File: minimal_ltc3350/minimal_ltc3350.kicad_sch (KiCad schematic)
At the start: 0 parts

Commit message: Update KiCad project files (PCB layout, project settings, and schematic)
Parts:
- added U1: LTC3350EUHF-PBF, analog_devices_footprints:QFN-38_UHF_LIT, symbol UNITED_IC_ADI:U_LTC3350EUHF-PBF
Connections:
- new net GND: U1.39 (PGND)
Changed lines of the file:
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@@
 	(generator "eeschema")
 	(generator_version "9.0")
-	(paper "A4")
+	(paper "A3")
+	(wire
+		(pts
+			(xy 203.2 231.14) (xy 203.2 232.41)
+		)
+		(stroke
+			(width 0)
+			(type default)
+		)
+	)
+	(symbol
+		(lib_id "UNITED_IC_ADI:U_LTC3350EUHF-PBF")
+		(at 203.2 152.4 0)
+		(unit 1)
+		(exclude_from_sim no)
+		(in_bom yes)
+		(on_board yes)
+		(dnp no)
+		(fields_autoplaced yes)
+		(property "Reference" "U1"
+			(at 205.3433 231.14 0)
+			(effects
+				(font
+					(size 1.524 1.524)
+				)
+				(justify left)
+			)
+		)
+		(property "Value" "LTC3350EUHF-PBF"
+			(at 205.3433 233.68 0)
+			(effects
+				(font
+					(size 1.524 1.524)
+				)
+				(justify left)
+			)
+		)
+		(property "Footprint" "analog_devices_footprints:QFN-38_UHF_LIT"
+			(at 243.84 236.22 0)
+			(effects
+				(font
+					(size 1.27 1.27)
+					(italic yes)
+				)
+				(justify left)
+				(hide yes)
+			)
+		)
+		(property "Datasheet" "https://www.analog.com/media/en/technical-documentation/data-sheets/ltc3350.pdf"
+			(at 243.84 231.14 0)
+			(effects
+				(font
+					(size 1.27 1.27)
+					(italic yes)
+				)
+				(justify left)
+				(hide yes)
+			)
+		)
+		(property "Description" "High Current Supercapacitor Backup Controller and System Monitor"
+			(at 243.84 233.68 0)
+			(effects
+				(font
+					(size 1.27 1.27)
+				)
+				(justify left)
+				(hide yes)
+			)
+		)
+		(property "MPN" "LTC3350EUHF#PBF"
+			(at 243.84 238.76 0)
+			(effects
+				(font
+					(size 1.27 1.27)
+				)
+				(justify left)
+				(hide yes)
+			)
+		)
+		(pin "26"
+		)
+		(pin "22"
+		)
+		(pin "4"
+		)
+		(pin "34"
+		)
+		(pin "35"
+		)
+		(pin "18"
+		)
+		(pin "30"
+		)
+		(pin "37"
+		)
+		(pin "28"
+		)
+		(pin "33"
+		)
+		(pin "24"
+		)
+		(pin "39"
+		)
+		(pin "17"
+		)
+		(pin "19"
+		)
+		(pin "5"
+		)
+		(pin "25"
+		)
+		(pin "2"
+		)
+		(pin "16"
+		)
+		(pin "14"
+		)
+		(pin "23"
+		)
+		(pin "11"
+		)
+		(pin "31"
+		)
+		(pin "7"
+		)
+		(pin "9"
+		)
+		(pin "20"
+		)
+		(pin "10"
+		)
+		(pin "29"
+		)
+		(pin "27"
+		)
+		(pin "1"
+		)
+		(pin "21"
+		)
+		(pin "15"
+		)
+		(pin "13"
+		)
+		(pin "32"
+		)
+		(pin "12"
+		)
+		(pin "3"
+		)
+		(pin "38"
+		)
+		(pin "36"
+		)
+		(pin "8"
+		)
+		(pin "6"
+		)
+		(instances
+			(project ""
+				(path "/7082067f-79ec-4bdc-ac64-cad75a2d3be3"
+					(reference "U1")
+					(unit 1)
+				)
+			)
+		)
+	)
+	(symbol
+		(lib_id "power:GND")
+		(at 203.2 232.41 0)
+		(unit 1)
+		(exclude_from_sim no)
+		(in_bom yes)
+		(on_board yes)
+		(dnp no)
+		(fields_autoplaced yes)
+		(property "Reference" "#PWR01"
+			(at 203.2 238.76 0)
+			(effects
+				(font
+					(size 1.27 1.27)
+				)
+				(hide yes)
+			)
+		)
+		(property "Value" "GND"
+			(at 203.2 237.49 0)
+			(effects
+				(font
+					(size 1.27 1.27)
+				)
+			)
+		)
+		(property "Footprint" ""
+			(at 203.2 232.41 0)
+			(effects
+				(font
+					(size 1.27 1.27)
+				)
+				(hide yes)
+			)
+		)
+		(property "Datasheet" ""
+			(at 203.2 232.41 0)
+			(effects
+				(font
+					(size 1.27 1.27)
+				)
+				(hide yes)
+			)
+		)
+		(property "Description" "Power symbol creates a global label with name \"GND\" , ground"
+			(at 203.2 232.41 0)
+			(effects
+				(font
+					(size 1.27 1.27)
+				)
+				(hide yes)
+			)
+		)
+		(pin "1"
+		)
+		(instances
+			(project ""
+				(path "/7082067f-79ec-4bdc-ac64-cad75a2d3be3"
+					(reference "#PWR01")
+					(unit 1)
+				)
+			)
+		)
+	)
 	(sheet_instances
 		(path "/"

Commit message: Update KiCad project files and submodule reference
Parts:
- added C1: 100 nF, capacitor_footprints:C_0402_1005Metric, symbol CAPACITORS_GCM155R71H_DATA_BASE:C_GCM155R71H104KE02D
- added C2: 1 µF, capacitor_footprints:C_0603_1608Metric, symbol CAPACITORS_GRM185R61E_DATA_BASE:C_GRM185R61E105KA12J
- added Q1: 20.0 V, transistor_footprints:PowerPAK 1212-8, symbol TRANSISTORS_SIS438DN-T1-GE3_DATA_BASE:Q_SIS438DN-T1-GE3
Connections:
- net GND: now also C1.2
- net VOUTSP: now reaches U1.31 (VOUTSP)
- net VOUTSP: now also C2.1, Q1.5 (D)
- net VOUTM5: now reaches U1.32 (VOUTM5)
- net VOUTM5: now also C2.2
- net INFET: now reaches U1.33 (INFET)
- net INFET: now also Q1.4 (G)
- net VIN: now reaches U1.34 (VIN)
- net VIN: now also C1.1, Q1.1 (S), Q1.2 (S), Q1.3 (S)

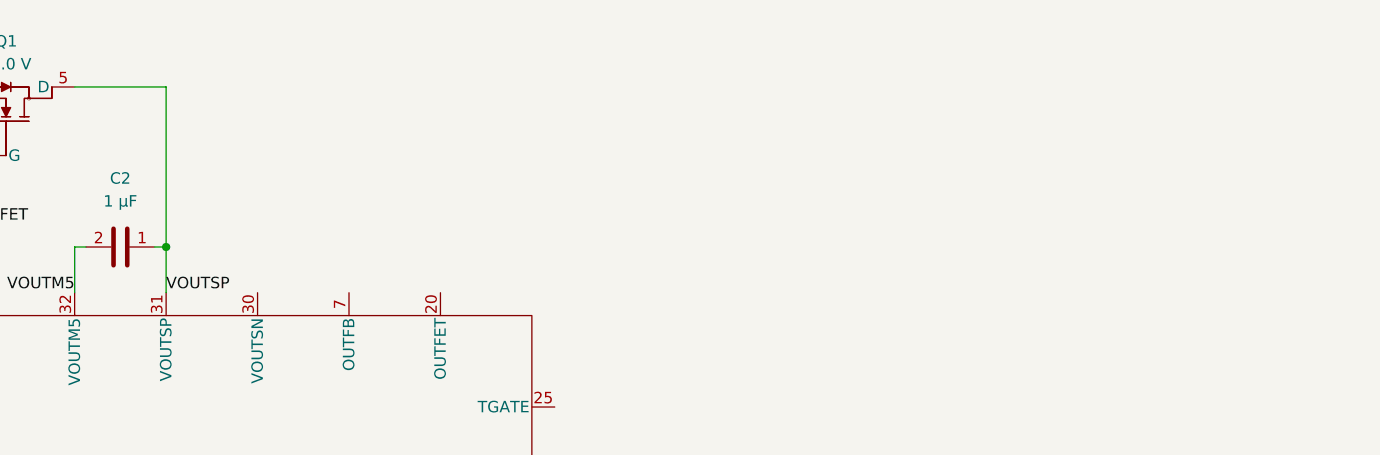
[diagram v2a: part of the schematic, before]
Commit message: Add VOUT sensing resistor and update symbol libraries
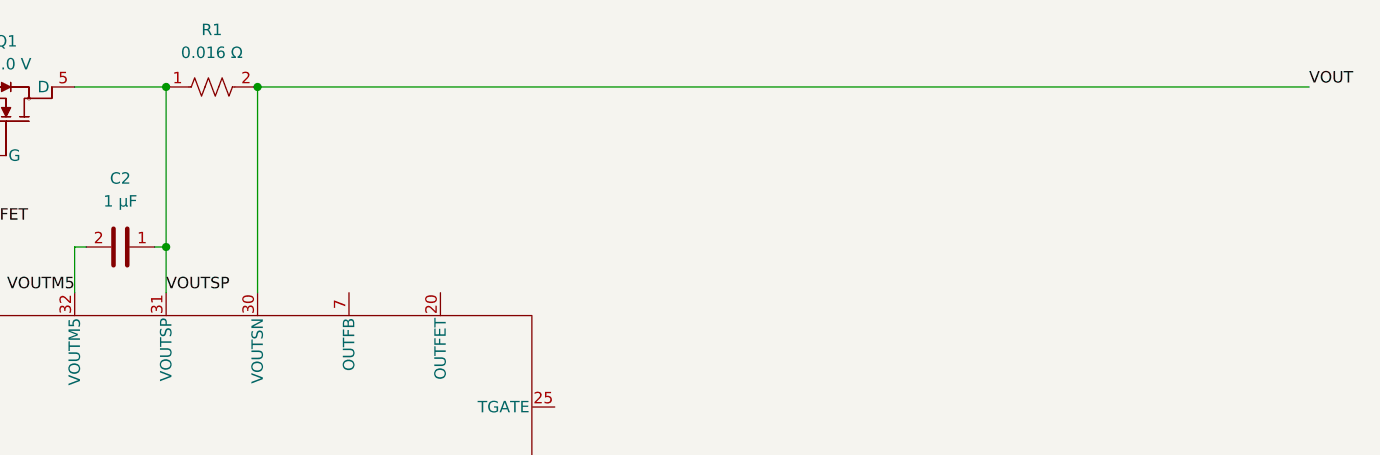
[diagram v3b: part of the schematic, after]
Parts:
- added R1: 0.016 Ω, resistor_footprints:R_0612_1632Metric, symbol RESISTORS_PRL1632-_DATA_BASE:R_PRL1632-R016-F-T1
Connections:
- net VOUTSP: now also R1.1
- net VOUT: now reaches U1.30 (VOUTSN)
- net VOUT: now also R1.2
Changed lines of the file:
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@@
+	)
+	(junction
+		(at 203.2 50.8)
+		(diameter 0)
+		(color 0 0 0 0)
 	)
 	(junction
@@
 	)
 	(junction
+		(at 213.36 50.8)
+		(diameter 0)
+		(color 0 0 0 0)
+	)
+	(junction
 		(at 175.26 53.34)
 		(diameter 0)
@@
 	(wire
 		(pts
+			(xy 213.36 50.8) (xy 213.36 73.66)
+		)
+		(stroke
+			(width 0)
+			(type default)
+		)
+	)
+	(wire
+		(pts
 			(xy 175.26 53.34) (xy 177.8 53.34)
 		)
@@
 		(pts
 			(xy 175.26 50.8) (xy 175.26 53.34)
+		)
+		(stroke
+			(width 0)
+			(type default)
+		)
+	)
+	(wire
+		(pts
+			(xy 213.36 50.8) (xy 330.2 50.8)
 		)
 		(stroke
@@
 	(label "VIN"
 		(at 172.72 66.04 0)
+		(effects
+			(font
+				(size 1.27 1.27)
+			)
+			(justify left bottom)
+		)
+	)
+	(label "VOUT"
+		(at 330.2 50.8 0)
 		(effects
 			(font
@@
 					(unit 1)
 				)
+			)
+		)
+	)
+	(symbol
+		(lib_id "RESISTORS_PRL1632-_DATA_BASE:R_PRL1632-R016-F-T1")
+		(at 208.28 50.8 0)
+		(unit 1)
+		(exclude_from_sim no)
+		(in_bom yes)
+		(on_board yes)
+		(dnp no)
+		(fields_autoplaced yes)
+		(property "Reference" "R1"
+			(at 208.28 44.45 0)
+			(effects
+				(font
+					(size 1.27 1.27)
+				)
+			)
+		)
+		(property "Value" "0.016 Ω"
+			(at 208.28 46.99 0)
+			(effects
+				(font
+					(size 1.27 1.27)
+				)
+			)
+		)
+		(property "Footprint" "resistor_footprints:R_0612_1632Metric"
+			(at 208.28 55.88 0)
+			(show_name yes)
+			(effects
+				(font
+					(size 1.27 1.27)
+				)
+				(justify left)
+				(hide yes)
+			)
+		)
+		(property "Datasheet" "https://www.susumu.co.jp/common/pdf/n_catalog_partition07_en.pdf"
+			(at 208.28 58.42 0)
+			(show_name yes)
+			(effects
+				(font
+					(size 1.27 1.27)
+				)
+				(justify left)
+				(hide yes)
+			)
+		)
+		(property "Description" "RES SMD 0.016 Ω 1% 0612"
+			(at 208.28 60.96 0)
+			(show_name yes)
+			(effects
+				(font
+					(size 1.27 1.27)
+				)
+				(justify left)
+				(hide yes)
+			)
+		)
+		(property "Case Code - in" "0612"
+			(at 208.28 63.5 0)
+			(show_name yes)
+			(effects
+				(font
+					(size 1.27 1.27)
+				)
+				(justify left)
+				(hide yes)
+			)
+		)
+		(property "Case Code - mm" "1632"
+			(at 208.28 66.04 0)
+			(show_name yes)
+			(effects
+				(font
+					(size 1.27 1.27)
+				)
+				(justify left)
+				(hide yes)
+			)
+		)
+		(property "Component Type" "Resistor"
+			(at 208.28 68.58 0)
+			(show_name yes)
+			(effects
+				(font
+					(size 1.27 1.27)
+				)
+				(justify left)
+				(hide yes)
+			)
+		)
+		(property "MPN" "PRL1632-R016-F-T1"
+			(at 208.28 71.12 0)
+			(show_name yes)
+			(effects
+				(font
+					(size 1.27 1.27)
+				)
+				(justify left)
+				(hide yes)
+			)
+		)
+		(property "Manufacturer" "Susumu"
+			(at 208.28 73.66 0)
+			(show_name yes)
+			(effects
+				(font
+					(size 1.27 1.27)
+				)
+				(justify left)
+				(hide yes)
+			)
+		)
+		(property "Series" "PRL1632-"
+			(at 208.28 76.2 0)
+			(show_name yes)
+			(effects
+				(font
+					(size 1.27 1.27)
+				)
+				(justify left)
+				(hide yes)
+			)
+		)
+		(property "Symbol Name" "R_PRL1632-R016-F-T1"
+			(at 208.28 78.74 0)
+			(show_name yes)
+			(effects
+				(font
+					(size 1.27 1.27)
+				)
+				(justify left)
+				(hide yes)
+			)
+		)
+		(property "Temperature Coefficient" ""
+			(at 208.28 81.28 0)
+			(show_name yes)
+			(effects
+				(font
+					(size 1.27 1.27)
+				)
+				(justify left)
+				(hide yes)
+			)
+		)
+		(property "Tolerance" "1%"
+			(at 208.28 83.82 0)
+			(show_name yes)
+			(effects
+				(font
+					(size 1.27 1.27)
+				)
+				(justify left)
+				(hide yes)
+			)
+		)
+		(property "Trustedparts Search" "https://www.trustedparts.com/en/search/PRL1632-R016-F-T1"
+			(at 208.28 86.36 0)
+			(show_name yes)
+			(effects
+				(font
+					(size 1.27 1.27)
+				)
+				(justify left)
+				(hide yes)
+			)
+		)
+		(property "Voltage Rating" ""
+			(at 208.28 88.9 0)
+			(show_name yes)
+			(effects
+				(font
+					(size 1.27 1.27)
+				)
+				(justify left)
+				(hide yes)
+			)
+		)
+		(pin "2"
+		)
+		(pin "1"
+		)
+		(instances
+			(project ""
+				(path "/7082067f-79ec-4bdc-ac64-cad75a2d3be3"
+					(reference "R1")
+					(unit 1)
+				)

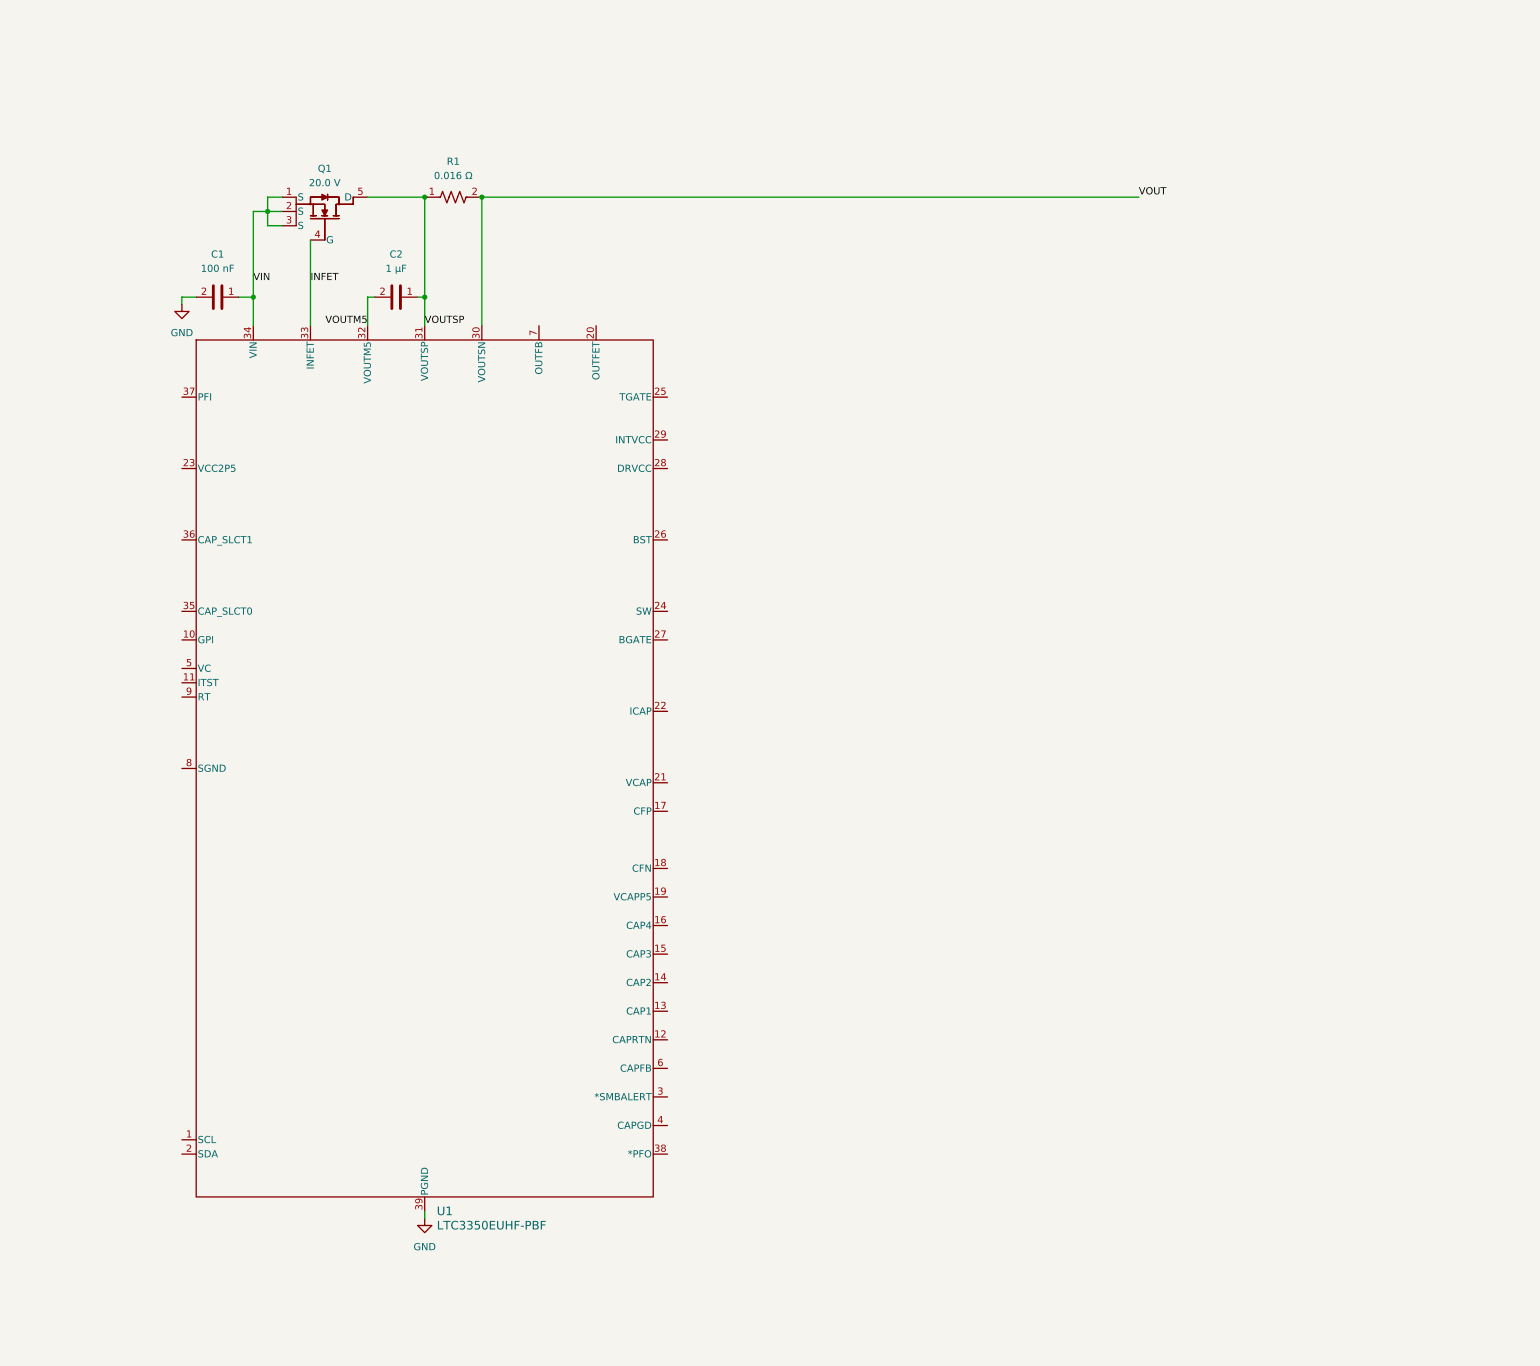
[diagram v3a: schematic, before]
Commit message: Update schematic and PCB with VOUT sensing resistor and component changes
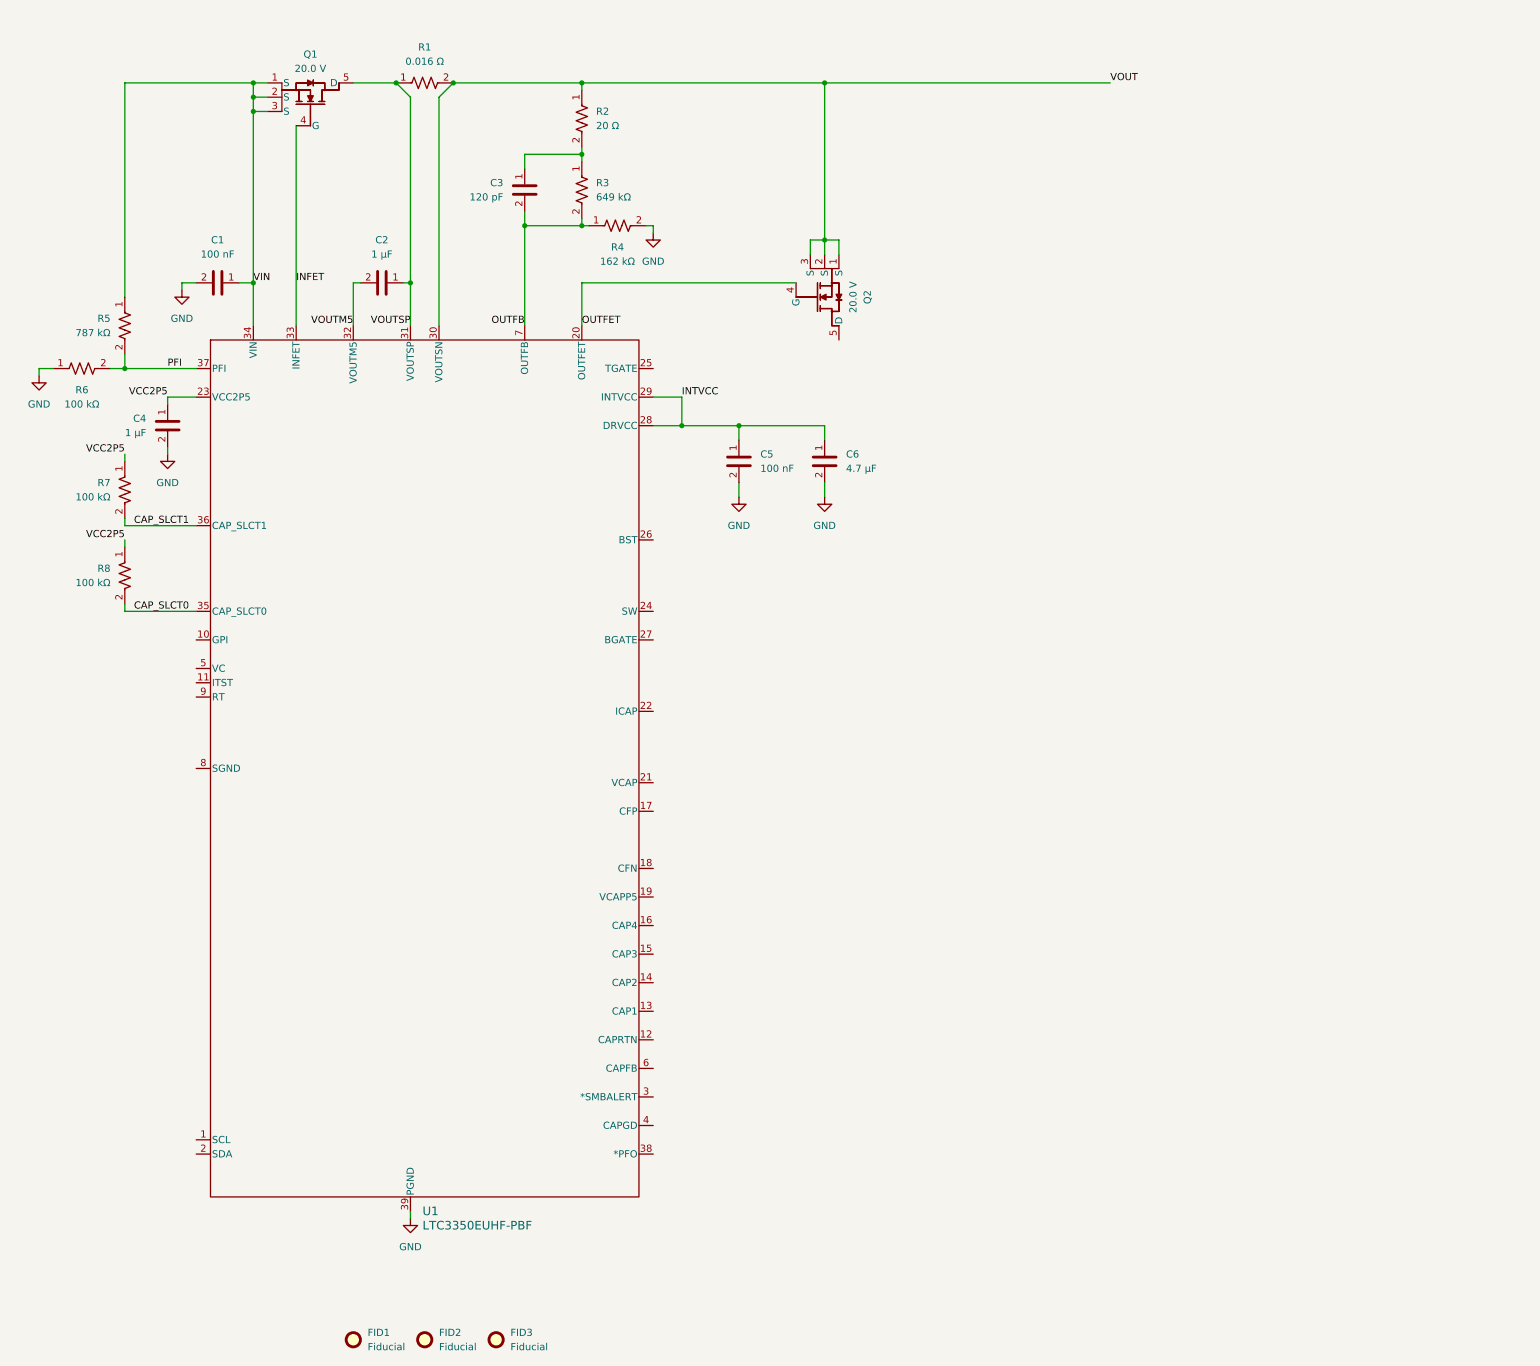
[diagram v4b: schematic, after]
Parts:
- added C3: 120 pF, capacitor_footprints:C_0402_1005Metric, symbol CAPACITORS_GCM1555C1H_DATA_BASE:C_GCM1555C1H121FA16D
- added C4: 1 µF, capacitor_footprints:C_0402_1005Metric, symbol CAPACITORS_C1005X6S1C_DATA_BASE:C_C1005X6S1C105K050BC
- added C5: 100 nF, capacitor_footprints:C_0402_1005Metric, symbol CAPACITORS_GCM155R71H_DATA_BASE:C_GCM155R71H104KE02D
- added C6: 4.7 µF, capacitor_footprints:C_0603_1608Metric, symbol CAPACITORS_GRM188C71A_DATA_BASE:C_GRM188C71A475KE11D
- added FID1, FID2, FID3: Fiducial, no_components_footprints:Fiducial_0.5mm_Mask1mm, symbol UNITED_NO_COMPONENTS_DATA_BASE:Fiducial
- added Q2: 20.0 V, transistor_footprints:PowerPAK 1212-8, symbol TRANSISTORS_SIS438DN-T1-GE3_DATA_BASE:Q_SIS438DN-T1-GE3
- added R2: 20 Ω, resistor_footprints:R_0402_1005Metric, symbol RESISTORS_ERJ-2RKF_DATA_BASE:R_ERJ-2RKF20R0X
- added R3: 649 kΩ, resistor_footprints:R_0402_1005Metric, symbol RESISTORS_ERJ-2RKF_DATA_BASE:R_ERJ-2RKF6493X
- added R4: 162 kΩ, resistor_footprints:R_0402_1005Metric, symbol RESISTORS_ERJ-2RKF_DATA_BASE:R_ERJ-2RKF1623X
- added R5: 787 kΩ, resistor_footprints:R_0402_1005Metric, symbol RESISTORS_ERJ-2RKF_DATA_BASE:R_ERJ-2RKF7873X
- added R6, R7, R8: 100 kΩ, resistor_footprints:R_0402_1005Metric, symbol RESISTORS_ERJ-2RKF_DATA_BASE:R_ERJ-2RKF1003X
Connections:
- net GND: now also C4.2, C5.2, C6.2, R4.2, R6.1
- net VIN: now also R5.1
- net VOUT: now also Q2.1 (S), Q2.2 (S), Q2.3 (S), R2.1
- net OUTFET: now reaches U1.20 (OUTFET)
- net OUTFET: now also Q2.4 (G)
- net VCC2P5: now reaches U1.23 (VCC2P5)
- net VCC2P5: now also C4.1, R7.1, R8.1
- net INTVCC: now reaches U1.28 (DRVCC)
- net INTVCC: now also U1.29 (INTVCC), C5.1, C6.1
- net CAP_SLCT0: now reaches U1.35 (CAP_SLCT0)
- net CAP_SLCT0: now also R8.2
- net CAP_SLCT1: now reaches U1.36 (CAP_SLCT1)
- net CAP_SLCT1: now also R7.2
- net PFI: now reaches U1.37 (PFI)
- net PFI: now also R5.2, R6.2
- net OUTFB: now reaches U1.7 (OUTFB)
- net OUTFB: now also C3.2, R3.2, R4.1
- new net: C3.1, R2.2, R3.1
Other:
- moved on the sheet: C1, C2, Q1, R1
